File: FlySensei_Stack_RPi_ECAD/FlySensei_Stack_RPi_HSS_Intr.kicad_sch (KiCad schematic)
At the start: 9 parts, among them J7 Conn_01x22_Female, J8 Conn_01x22_Female, J9 Conn_01x14_Female, U8 TPD4EUSB30, U9 TPD4EUSB30

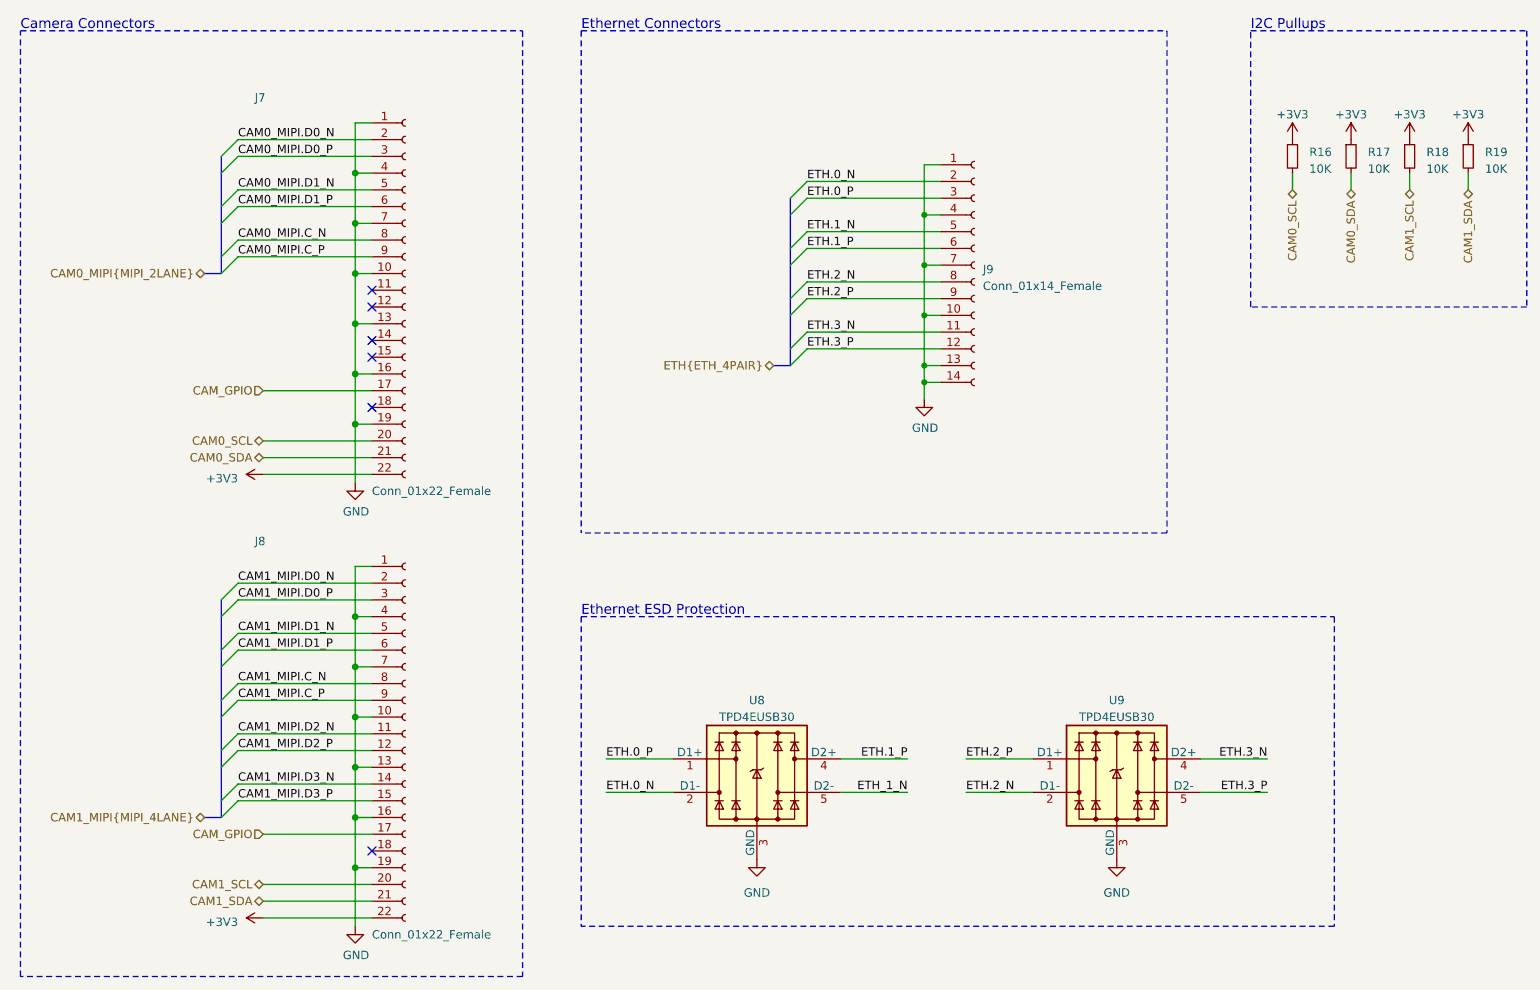
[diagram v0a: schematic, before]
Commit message: PCB Design for the Raspberry PI CM4 Board (V0.1)
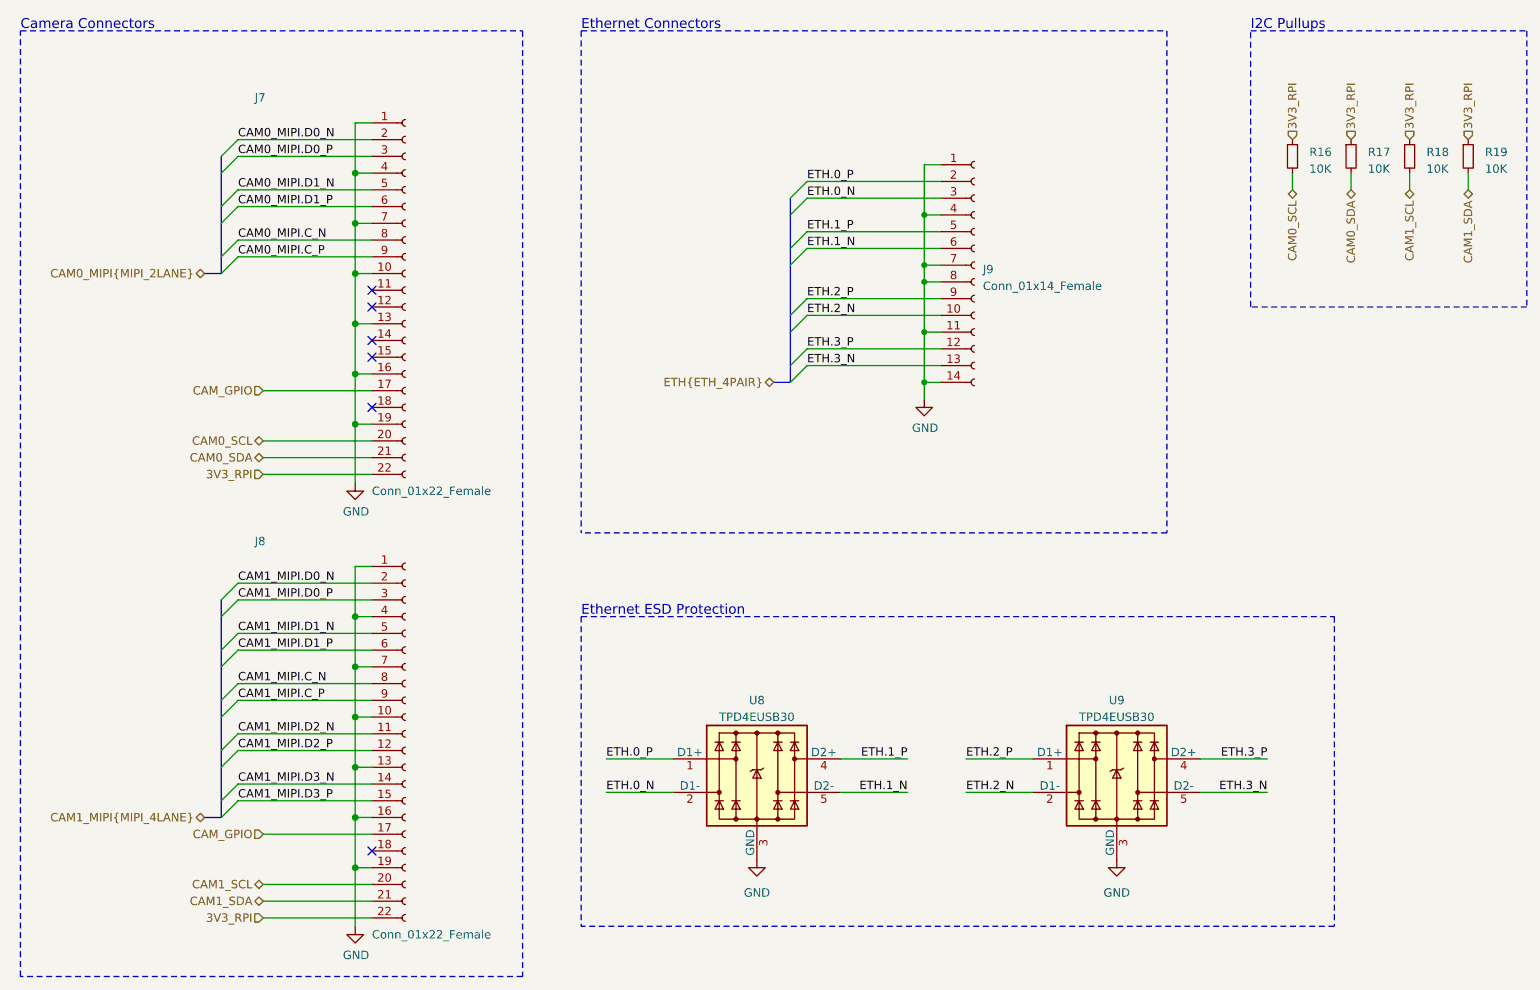
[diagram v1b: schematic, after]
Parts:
- J9: footprint (none) -> Connector_FFC-FPC:Hirose_FH12-14S-0.5SH_1x14-1MP_P0.50mm_Horizontal
- R16, R17, R18, R19: footprint (none) -> Resistor_SMD:R_0402_1005Metric
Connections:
- net ETH_1_N is gone; now on net ETH.1_N: U8.5 (D2-)
- net ETH.0_N: now also J9.3 (Pin_3); no longer J9.2 (Pin_2)
- net ETH.0_P: now also J9.2 (Pin_2); no longer J9.3 (Pin_3)
- net ETH.1_N: now also J9.6 (Pin_6); no longer J9.5 (Pin_5)
- net ETH.1_P: now also J9.5 (Pin_5); no longer J9.6 (Pin_6)
- net ETH.2_N: now also J9.10 (Pin_10); no longer J9.8 (Pin_8)
- net ETH.3_N: now also J9.13 (Pin_13), U9.5 (D2-); no longer J9.11 (Pin_11), U9.4 (D2+)
- net ETH.3_P: now also U9.4 (D2+); no longer U9.5 (D2-)
- net GND: now also J9.11 (Pin_11), J9.8 (Pin_8); no longer J9.10 (Pin_10), J9.13 (Pin_13)
- net +3V3 renamed 3V3_RPI
